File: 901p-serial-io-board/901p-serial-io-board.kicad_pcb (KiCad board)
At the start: 2 copper layers, 5 parts, among them J1 DE15, J2 DE9_Socket, J3 Barrel_Jack_MountingPin, J4 V+, J5 V-

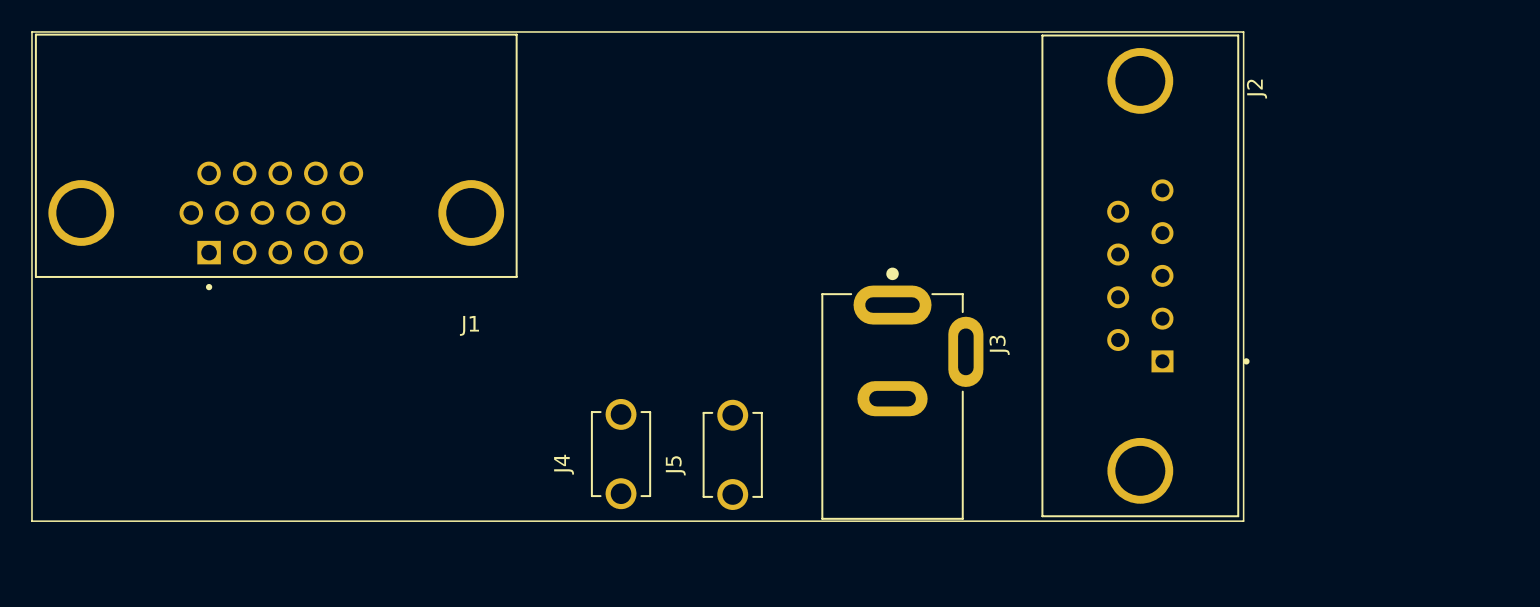
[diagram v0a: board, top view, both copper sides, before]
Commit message: fix board pinout, add analog headers
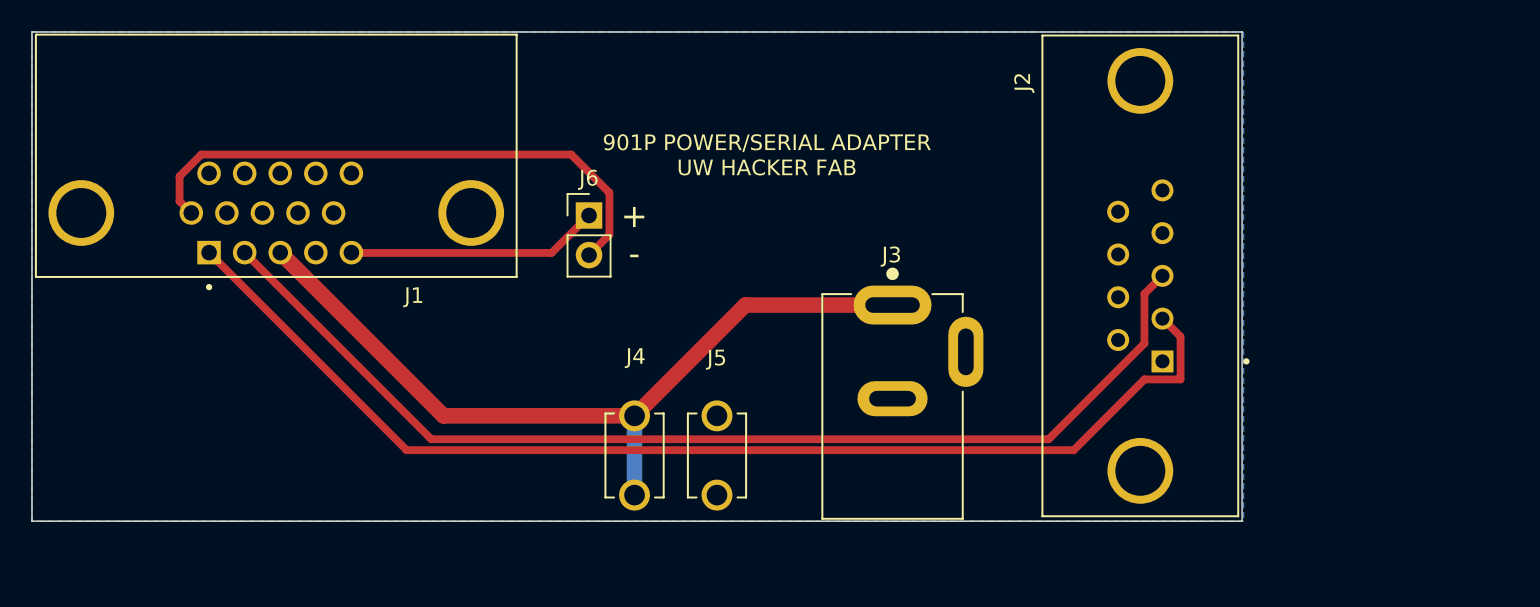
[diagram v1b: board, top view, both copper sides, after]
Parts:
- added J6: ANALOG, Connector_PinHeader_2.54mm:PinHeader_1x02_P2.54mm_Vertical, F.Cu at (112.0, 64.5)
- J1: value DE15 -> DE15 (SENSOR)
- J2: value DE9_Socket -> DE9 (RS-232)
- J3: value Barrel_Jack_MountingPin -> BARREL (9-30V)
- moved J5 1.01 mm to (120.2, 79.8)
- moved J4 0.87 mm to (114.9, 79.8)
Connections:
- J1 pad 4: Net-(J3-MountPin) -> GND
- J1 pad 5: unconnected-(J1-Pad5) -> Net-(J6-Pin_1)
- J1 pad 6: unconnected-(J1-Pad6) -> Net-(J6-Pin_2)
- J2 pad 2: unconnected-(J2-Pad2) -> Net-(J1-Pad1)
- J2 pad 3: unconnected-(J2-Pad3) -> Net-(J1-Pad2)
- J2 pad 5: unconnected-(J2-Pad5) -> GND
- J2 pad 6: Net-(J1-Pad1) -> unconnected-(J2-Pad6)
- J2 pad 7: Net-(J1-Pad2) -> unconnected-(J2-Pad7)
- J2 pad 9: Net-(J3-MountPin) -> unconnected-(J2-Pad9)
- J3 pad 2: Net-(J3-MountPin) -> GND
- J3 pad MP: Net-(J3-MountPin) -> GND
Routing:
- net Net-(J1-Pad1): track 0.00 -> 74.1 mm
- net Net-(J1-Pad2): track 0.00 -> 70.0 mm
- net Net-(J4-Pin_1): track 0.00 -> 51.6 mm
- net Net-(J6-Pin_2): track 0.00 -> 36.3 mm
- net Net-(J6-Pin_1): track 0.00 -> 16.2 mm
- added copper zone on B.Cu, net GND
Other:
- board outline added: 77.5 x 31.3 mm
- board text added: "+ -"
- board text added: "901P POWER/SERIAL ADAPTER UW HACKER FAB"

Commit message: ok final reroute for real
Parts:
- J2: footprint DE9_Amphenol_LD09S24A4GV00LF:AMPHENOL_LD09S24A4GV00LF -> DE9_Amphenol_LD09S33E4GV00LF:AMPHENOL_LD09S33E4GV00LF
- moved J2 2.93 mm to (144.4, 68.3), turned to 90 degrees
- moved J6 2.34 mm to (112.1, 66.8), turned to 180 degrees
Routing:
- net Net-(J1-Pad2): track 70.0 -> 58.2 mm
- net Net-(J6-Pin_2): track 36.3 -> 27.7 mm
- net Net-(J1-Pad1): track 74.1 -> 67.8 mm
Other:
- board text added: "- +"
- board text removed: "+ -"

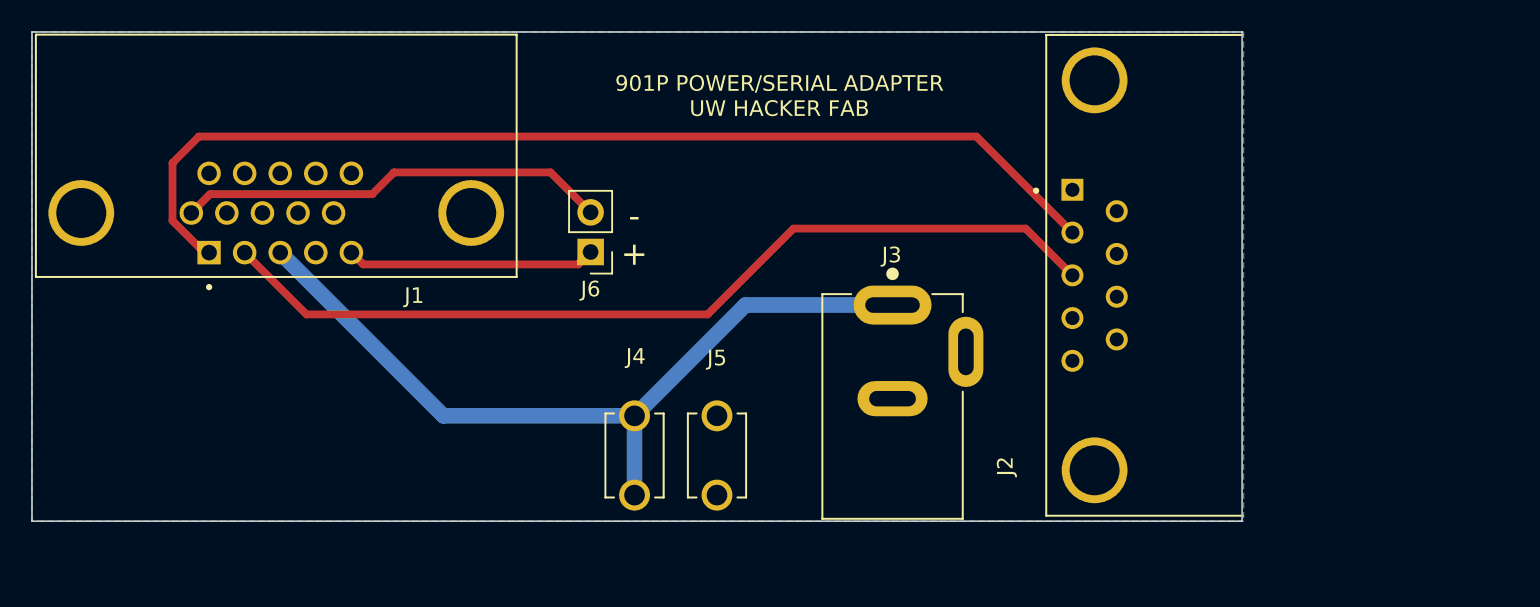
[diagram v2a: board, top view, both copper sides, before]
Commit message: miniaturized board
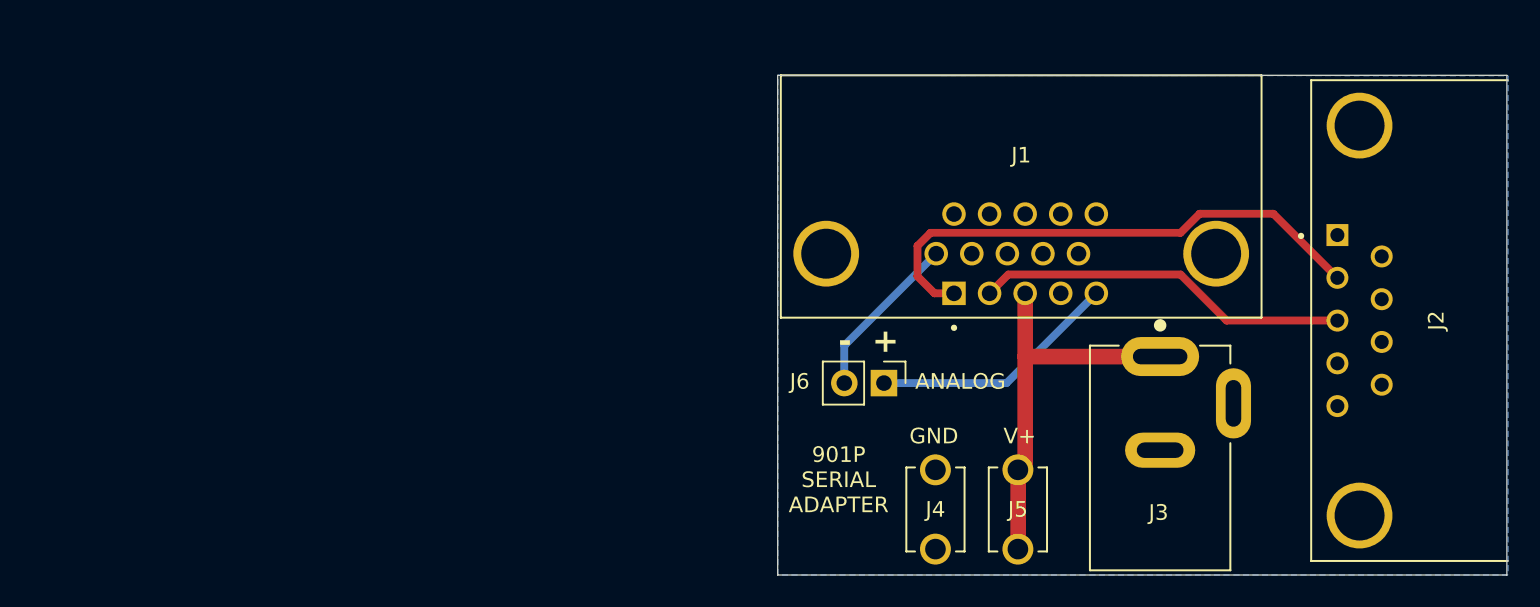
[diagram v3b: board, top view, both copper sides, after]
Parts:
- moved J1 47.8 mm to (139.7, 66.9)
- moved J4 24.8 mm to (139.5, 83.3), turned to -90 degrees
- moved J6 20.6 mm to (130.9, 75.2), turned to -90 degrees
- moved J3 17.5 mm to (148.6, 73.5)
- moved J2 17.2 mm to (161.4, 71.2)
- moved J5 14.4 mm to (134.2, 83.3), turned to -90 degrees
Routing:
- net Net-(J1-Pad2): track 58.2 -> 24.0 mm
- net Net-(J1-Pad1): track 67.8 -> 34.2 mm
- net Net-(J4-Pin_1): track 51.6 -> 25.2 mm
- net Net-(J6-Pin_2): track 27.7 -> 10.7 mm
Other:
- board size 77.5 x 31.3 mm -> 46.7 x 32 mm
- board text added: "+"
- board text added: "-"
- board text added: "901P SERIAL ADAPTER"
- board text added: "ANALOG"
- board text added: "GND"
- board text added: "V+"
- board text removed: "- +"
- board text removed: "901P POWER/SERIAL ADAPTER UW HACKER FAB"

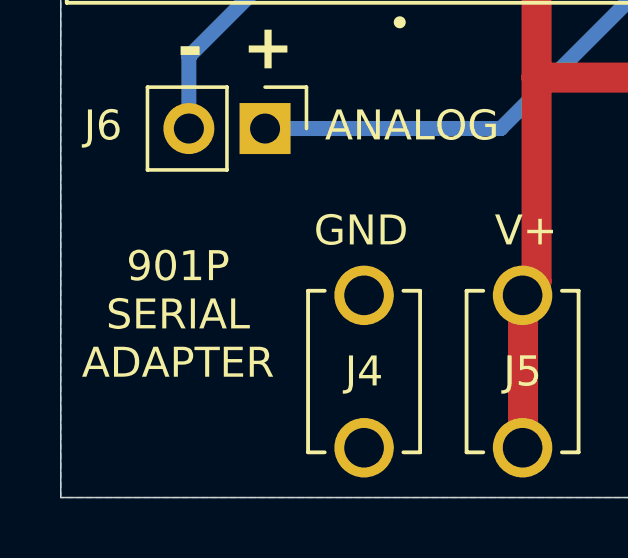
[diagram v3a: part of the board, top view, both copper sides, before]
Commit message: re-add labelling on back side
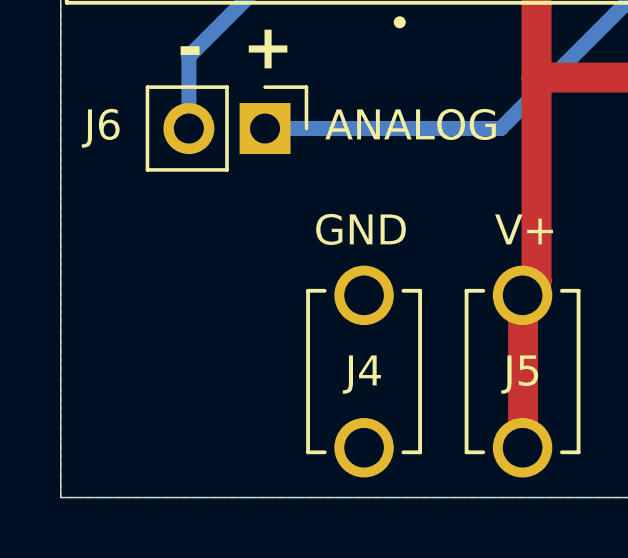
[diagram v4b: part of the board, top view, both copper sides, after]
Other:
- board text added: "901P SERIAL/ANALOG ADAPTER v0.1 POWER: +9-30 VDC"
- board text removed: "901P SERIAL ADAPTER"
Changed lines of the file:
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@@
 		(layer "Edge.Cuts")
-	)
-	(gr_text "901P\nSERIAL\nADAPTER"
-		(at 128 81.4 0)
-		(layer "F.SilkS")
-		(effects
-			(font
-				(size 1 1)
-				(thickness 0.15)
-			)
-		)
 	)
 	(gr_text "ANALOG"
@@
 		)
 	)
+	(gr_text "901P SERIAL/ANALOG ADAPTER v0.1\nPOWER: +9-30 VDC"
+		(at 140 58.8 0)
+		(layer "B.SilkS")
+		(effects
+			(font
+				(size 1 1)
+				(thickness 0.15)
+			)
+			(justify mirror)
+		)
+	)
